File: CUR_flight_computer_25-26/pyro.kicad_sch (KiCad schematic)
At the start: 26 parts, among them J10 PYRO, J11 PYRO, J8 PYRO, J9 PYRO, U12 BUK9K25-40RAX, U13 BUK9K25-40RAX

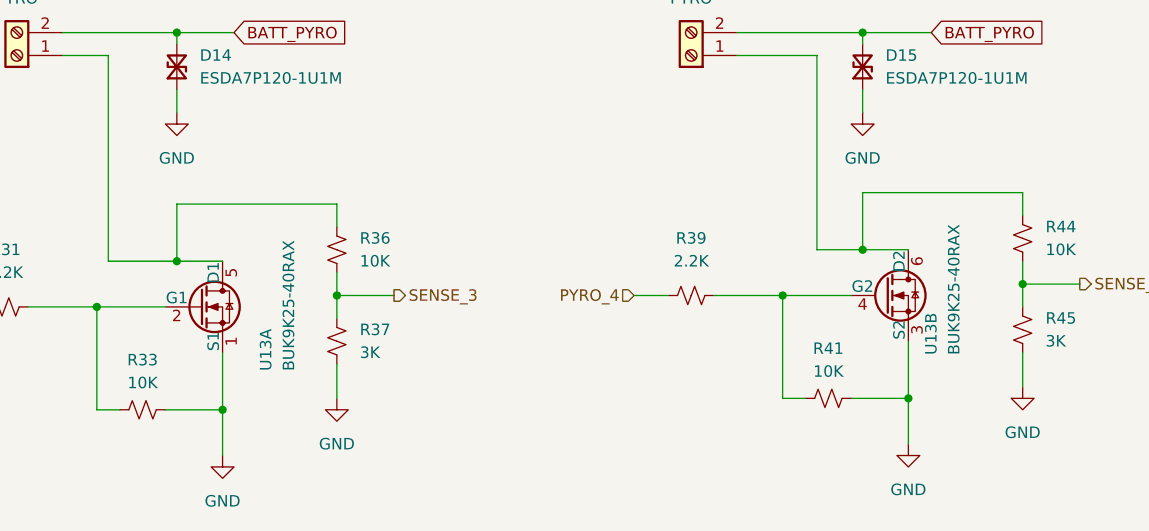
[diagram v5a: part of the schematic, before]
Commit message: started routing power and rf section
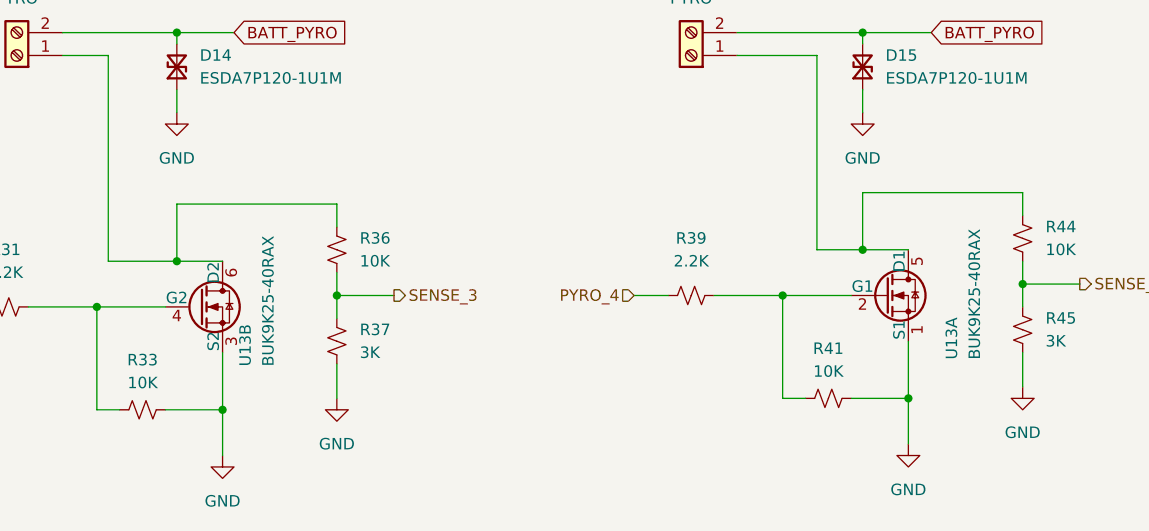
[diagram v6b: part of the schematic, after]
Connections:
- net at J9.1 (Pin_1), R36.1: now also U13.6 (D2); no longer U13.5 (D1)
- net at J11.1 (Pin_1), R44.1: now also U13.5 (D1); no longer U13.6 (D2)
- net at R39.2, R41.1: now also U13.2 (G1); no longer U13.4 (G2)
- net at R31.2, R33.1: now also U13.4 (G2); no longer U13.2 (G1)
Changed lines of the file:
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@@
+	)
+	(symbol
+		(lib_id "BUK9K25-40RAX:BUK9K25-40RAX")
+		(at 151.13 139.7 0)
+		(unit 1)
+		(exclude_from_sim no)
+		(in_bom yes)
+		(on_board yes)
+		(dnp no)
+		(property "Reference" "U13"
+			(at 155.956 146.812 90)
+			(effects
+				(font
+					(size 1.27 1.27)
+				)
+				(justify left)
+			)
+		)
+		(property "Value" "BUK9K25-40RAX"
+			(at 158.496 146.812 90)
+			(effects
+				(font
+					(size 1.27 1.27)
+				)
+				(justify left)
+			)
+		)
+		(property "Footprint" "BUK9K25-40RAX:BUK9K2540RAX"
+			(at 151.13 139.7 0)
+			(effects
+				(font
+					(size 1.27 1.27)
+				)
+				(hide yes)
+			)
+		)
+		(property "Datasheet" "https://assets.nexperia.com/documents/data-sheet/BUK9K25-40RA.pdf"
+			(at 151.13 139.7 0)
+			(effects
+				(font
+					(size 1.27 1.27)
+				)
+				(hide yes)
+			)
+		)
+		(property "Description" "Nexperia USA Mosfet Array 40V 18.2A 2 N Channel NMOS"
+			(at 151.13 139.7 0)
+			(effects
+				(font
+					(size 1.27 1.27)
+				)
+				(hide yes)
+			)
+		)
+		(pin "4"
+		)
+		(pin "6"
+		)
+		(pin "1"
+		)
+		(pin "5"
+		)
+		(pin "3"
+		)
+		(pin "2"
+		)
+		(instances
+			(project "CUR_flight_computer_25-26"
+				(path "/bf7761cc-1b32-4d86-809c-5f027005229b/a6095a4d-1542-4c9d-ab0b-9ed076818c96"
+					(reference "U13")
+					(unit 1)
+				)
+			)
+		)
 	)
 	(symbol
@@
 	)
 	(symbol
+		(lib_id "BUK9K25-40RAX:BUK9K25-40RAX")
+		(at 74.93 140.97 0)
+		(unit 2)
+		(exclude_from_sim no)
+		(in_bom yes)
+		(on_board yes)
+		(dnp no)
+		(property "Reference" "U13"
+			(at 77.47 147.574 90)
+			(effects
+				(font
+					(size 1.27 1.27)
+				)
+				(justify left)
+			)
+		)
+		(property "Value" "BUK9K25-40RAX"
+			(at 80.01 147.574 90)
+			(effects
+				(font
+					(size 1.27 1.27)
+				)
+				(justify left)
+			)
+		)
+		(property "Footprint" "BUK9K25-40RAX:BUK9K2540RAX"
+			(at 74.93 140.97 0)
+			(effects
+				(font
+					(size 1.27 1.27)
+				)
+				(hide yes)
+			)
+		)
+		(property "Datasheet" "https://assets.nexperia.com/documents/data-sheet/BUK9K25-40RA.pdf"
+			(at 74.93 140.97 0)
+			(effects
+				(font
+					(size 1.27 1.27)
+				)
+				(hide yes)
+			)
+		)
+		(property "Description" "Nexperia USA Mosfet Array 40V 18.2A 2 N Channel NMOS"
+			(at 74.93 140.97 0)
+			(effects
+				(font
+					(size 1.27 1.27)
+				)
+				(hide yes)
+			)
+		)
+		(pin "4"
+		)
+		(pin "6"
+		)
+		(pin "1"
+		)
+		(pin "5"
+		)
+		(pin "3"
+		)
+		(pin "2"
+		)
+		(instances
+			(project "CUR_flight_computer_25-26"
+				(path "/bf7761cc-1b32-4d86-809c-5f027005229b/a6095a4d-1542-4c9d-ab0b-9ed076818c96"
+					(reference "U13")
+					(unit 2)
+				)
+			)
+		)
+	)
+	(symbol
 		(lib_id "power:GND")
 		(at 163.83 149.86 0)
@@
 	)
 	(symbol
-		(lib_id "BUK9K25-40RAX:BUK9K25-40RAX")
-		(at 151.13 139.7 0)
-		(unit 2)
-		(exclude_from_sim no)
-		(in_bom yes)
-		(on_board yes)
-		(dnp no)
-		(property "Reference" "U13"
-			(at 153.67 146.304 90)
-			(effects
-				(font
-					(size 1.27 1.27)
-				)
-				(justify left)
-			)
-		)
-		(property "Value" "BUK9K25-40RAX"
-			(at 156.21 146.304 90)
-			(effects
-				(font
-					(size 1.27 1.27)
-				)
-				(justify left)
-			)
-		)
-		(property "Footprint" "BUK9K25-40RAX:BUK9K2540RAX"
-			(at 151.13 139.7 0)
-			(effects
-				(font
-					(size 1.27 1.27)
-				)
-				(hide yes)
-			)
-		)
-		(property "Datasheet" "https://assets.nexperia.com/documents/data-sheet/BUK9K25-40RA.pdf"
-			(at 151.13 139.7 0)
-			(effects
-				(font
-					(size 1.27 1.27)
-				)
-				(hide yes)
-			)
-		)
-		(property "Description" "Nexperia USA Mosfet Array 40V 18.2A 2 N Channel NMOS"
-			(at 151.13 139.7 0)
-			(effects
-				(font
-					(size 1.27 1.27)
-				)
-				(hide yes)
-			)
-		)
-		(pin "4"
-		)
-		(pin "6"
-		)
-		(pin "1"
-		)
-		(pin "5"
-		)
-		(pin "3"
-		)
-		(pin "2"
-		)
-		(instances
-			(project "CUR_flight_computer_25-26"
-				(path "/bf7761cc-1b32-4d86-809c-5f027005229b/a6095a4d-1542-4c9d-ab0b-9ed076818c96"
-					(reference "U13")
-					(unit 2)
-				)
-			)
-		)
-	)
-	(symbol
 		(lib_id "Device:R_Small_US")
 		(at 87.63 63.5 0)
@@
 					(unit 1)
 				)
-			)
-		)
-	)
-	(symbol
-		(lib_id "BUK9K25-40RAX:BUK9K25-40RAX")
-		(at 74.93 140.97 0)
-		(unit 1)
-		(exclude_from_sim no)
-		(in_bom yes)
-		(on_board yes)
-		(dnp no)
-		(property "Reference" "U13"
-			(at 79.756 148.082 90)
-			(effects
-				(font
-					(size 1.27 1.27)
-				)
-				(justify left)
-			)
-		)
-		(property "Value" "BUK9K25-40RAX"
-			(at 82.296 148.082 90)
-			(effects
-				(font
-					(size 1.27 1.27)
-				)
-				(justify left)
-			)
-		)
-		(property "Footprint" "BUK9K25-40RAX:BUK9K2540RAX"
-			(at 74.93 140.97 0)
-			(effects
-				(font
-					(size 1.27 1.27)
-				)
-				(hide yes)
-			)
-		)
-		(property "Datasheet" "https://assets.nexperia.com/documents/data-sheet/BUK9K25-40RA.pdf"
-			(at 74.93 140.97 0)
-			(effects
-				(font
-					(size 1.27 1.27)
-				)
-				(hide yes)
-			)
-		)
-		(property "Description" "Nexperia USA Mosfet Array 40V 18.2A 2 N Channel NMOS"
-			(at 74.93 140.97 0)
-			(effects
-				(font
-					(size 1.27 1.27)
-				)
-				(hide yes)
-			)
-		)
-		(pin "4"
-		)
-		(pin "6"
-		)
-		(pin "1"
-		)
-		(pin "5"
-		)
-		(pin "3"
-		)
-		(pin "2"
-		)
-		(instances
-			(project "CUR_flight_computer_25-26"
-				(path "/bf7761cc-1b32-4d86-809c-5f027005229b/a6095a4d-1542-4c9d-ab0b-9ed076818c96"
-					(reference "U13")
-					(unit 1)
-				)

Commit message: routed all the debug lines!
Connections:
- net BATT_PYRO: now also J11.1 (Pin_1), J9.1 (Pin_1); no longer J11.2 (Pin_2), J9.2 (Pin_2)
- net at R44.1, U13.5 (D1): now also J11.2 (Pin_2); no longer J11.1 (Pin_1)
- net at R36.1, U13.6 (D2): now also J9.2 (Pin_2); no longer J9.1 (Pin_1)
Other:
- moved on the sheet: J11, J9
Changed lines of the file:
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@@
+	(wire
+		(pts
+			(xy 57.15 113.03) (xy 62.23 113.03)
+		)
+		(stroke
+			(width 0)
+			(type default)
+		)
+	)
 	(wire
 		(pts
@@
 	(wire
 		(pts
+			(xy 132.08 113.03) (xy 140.97 113.03)
+		)
+		(stroke
+			(width 0)
+			(type default)
+		)
+	)
+	(wire
+		(pts
 			(xy 163.83 138.43) (xy 163.83 140.97)
 		)
@@
 		(pts
 			(xy 151.13 82.55) (xy 151.13 87.63)
-		)
-		(stroke
-			(width 0)
-			(type default)
-		)
-	)
-	(wire
-		(pts
-			(xy 132.08 113.03) (xy 140.97 113.03)
-		)
-		(stroke
-			(width 0)
-			(type default)
-		)
-	)
-	(wire
-		(pts
-			(xy 62.23 113.03) (xy 57.15 113.03)
 		)
 		(stroke
@@
 	(symbol
 		(lib_id "Connector:Screw_Terminal_01x02")
-		(at 52.07 113.03 180)
+		(at 52.07 110.49 0)
+		(mirror y)
 		(unit 1)
 		(exclude_from_sim no)
@@
 		(on_board yes)
 		(dnp no)
-		(fields_autoplaced yes)
 		(property "Reference" "J9"
-			(at 52.07 104.14 0)
+			(at 52.07 119.38 0)
 			(effects
 				(font
@@
 		)
 		(property "Value" "PYRO"
-			(at 52.07 106.68 0)
+			(at 52.07 116.84 0)
 			(effects
 				(font
@@
 		)
 		(property "Footprint" "Terminal_SAMESKY_TB0011-350-02GR:SAMESKY_TB0011-350-02GR"
-			(at 52.07 113.03 0)
+			(at 52.07 110.49 0)
 			(effects
 				(font
@@
 		)
 		(property "Datasheet" "~"
-			(at 52.07 113.03 0)
+			(at 52.07 110.49 0)
 			(effects
 				(font
@@
 		)
 		(property "Description" "Generic screw terminal, single row, 01x02, script generated (kicad-library-utils/schlib/autogen/connector/)"
-			(at 52.07 113.03 0)
+			(at 52.07 110.49 0)
 			(effects
 				(font
@@
 	(symbol
 		(lib_id "Connector:Screw_Terminal_01x02")
-		(at 127 113.03 180)
+		(at 127 110.49 0)
+		(mirror y)
 		(unit 1)
 		(exclude_from_sim no)
@@
 		(on_board yes)
 		(dnp no)
-		(fields_autoplaced yes)
 		(property "Reference" "J11"
-			(at 127 104.14 0)
+			(at 127 119.38 0)
 			(effects
 				(font
@@
 		)
 		(property "Value" "PYRO"
-			(at 127 106.68 0)
+			(at 127 116.84 0)
 			(effects
 				(font
@@
 		)
 		(property "Footprint" "Terminal_SAMESKY_TB0011-350-02GR:SAMESKY_TB0011-350-02GR"
-			(at 127 113.03 0)
+			(at 127 110.49 0)
 			(effects
 				(font
@@
 		)
 		(property "Datasheet" "~"
-			(at 127 113.03 0)
+			(at 127 110.49 0)
 			(effects
 				(font
@@
 		)
 		(property "Description" "Generic screw terminal, single row, 01x02, script generated (kicad-library-utils/schlib/autogen/connector/)"
-			(at 127 113.03 0)
-			(effects
-				(font
+			(at 127 110.49 0)
+			(effects
+				(font

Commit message: Layout power and pyro
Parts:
- removed D13, D14, D15, D16: ESDA7P120-1U1M, ESDA7P120:TVS_ESDA7P120-1U1M, symbol Device:D_TVS_Small
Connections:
- net BATT_PYRO: now also J8.1 (Pin_1); no longer J8.2 (Pin_2)
- net at R34.1, U12.5 (D1): now also J8.2 (Pin_2); no longer J8.1 (Pin_1)
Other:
- moved on the sheet: J8
